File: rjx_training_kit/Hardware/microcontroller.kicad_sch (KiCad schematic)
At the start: 15 parts, among them SW2 SW_Push, U9 STM32L431RCTx, Y1 8MHz

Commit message: [RJX]: Initial footprint assignment. This is subject to further review and analysis.
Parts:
- C15, C16, C17, C18, C19, C20, C21, C22, C23, C24, C25: footprint (none) -> Capacitor_SMD:C_0603_1608Metric
- R41: footprint (none) -> Resistor_SMD:R_0603_1608Metric
- SW2: footprint (none) -> Button_Switch_THT:SW_PUSH_6mm
- Y1: footprint (none) -> Crystal:Crystal_SMD_3225-4Pin_3.2x2.5mm
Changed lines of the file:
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@@
 			)
 		)
-		(property "Footprint" ""
+		(property "Footprint" "Capacitor_SMD:C_0603_1608Metric"
 			(at 86.6648 52.07 0)
 			(effects
@@
 			)
 		)
-		(property "Footprint" ""
+		(property "Footprint" "Capacitor_SMD:C_0603_1608Metric"
 			(at 47.2948 80.01 0)
 			(effects
@@
 			)
 		)
-		(property "Footprint" ""
+		(property "Footprint" "Capacitor_SMD:C_0603_1608Metric"
 			(at 68.8848 96.52 0)
 			(effects
@@
 			)
 		)
-		(property "Footprint" ""
+		(property "Footprint" "Crystal:Crystal_SMD_3225-4Pin_3.2x2.5mm"
 			(at 62.23 85.09 0)
 			(effects
@@
 			)
 		)
-		(property "Footprint" ""
+		(property "Footprint" "Capacitor_SMD:C_0603_1608Metric"
 			(at 53.6448 96.52 0)
 			(effects
@@
 			)
 		)
-		(property "Footprint" ""
+		(property "Footprint" "Resistor_SMD:R_0603_1608Metric"
 			(at 86.614 85.344 90)
 			(effects
@@
 			)
 		)
-		(property "Footprint" ""
+		(property "Footprint" "Capacitor_SMD:C_0603_1608Metric"
 			(at 132.3848 52.07 0)
 			(effects
@@
 			)
 		)
-		(property "Footprint" ""
+		(property "Footprint" "Capacitor_SMD:C_0603_1608Metric"
 			(at 120.9548 52.07 0)
 			(effects
@@
 			)
 		)
-		(property "Footprint" ""
+		(property "Footprint" "Capacitor_SMD:C_0603_1608Metric"
 			(at 98.0948 52.07 0)
 			(effects
@@
 			)
 		)
-		(property "Footprint" ""
+		(property "Footprint" "Capacitor_SMD:C_0603_1608Metric"
 			(at 174.2948 52.07 0)
 			(effects
@@
 			)
 		)
-		(property "Footprint" ""
+		(property "Footprint" "Capacitor_SMD:C_0603_1608Metric"
 			(at 109.5248 52.07 0)
 			(effects
@@
 			)
 		)
-		(property "Footprint" ""
+		(property "Footprint" "Button_Switch_THT:SW_PUSH_6mm"
 			(at 33.02 76.2 0)
 			(effects
@@
 			)
 		)
-		(property "Footprint" ""
+		(property "Footprint" "Capacitor_SMD:C_0603_1608Metric"
 			(at 164.1348 52.07 0)
 			(effects
@@
 			)
 		)
-		(property "Footprint" ""
+		(property "Footprint" "Capacitor_SMD:C_0603_1608Metric"
 			(at 143.8148 52.07 0)
 			(effects

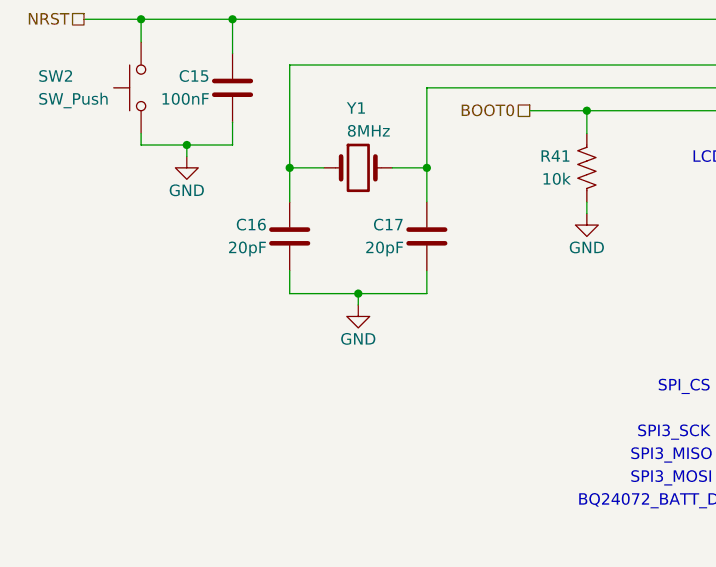
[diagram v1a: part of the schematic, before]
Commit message: [RJX]: Updated load capacitance values
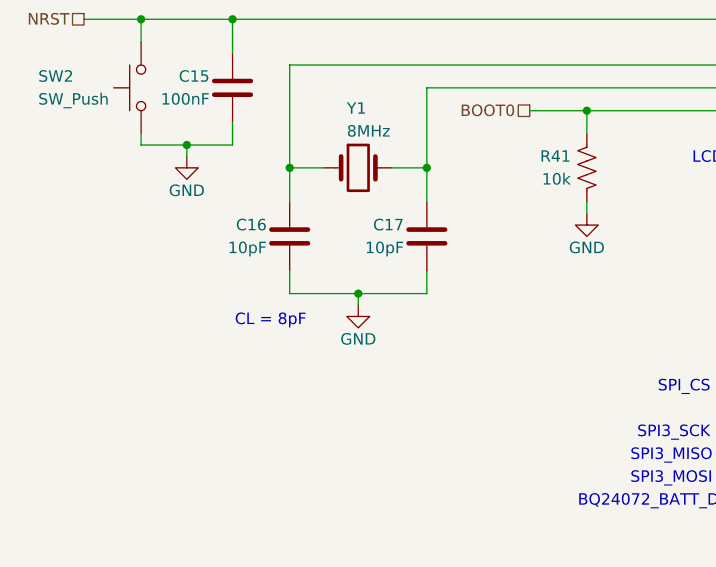
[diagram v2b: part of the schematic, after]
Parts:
- C16, C17: value 20pF -> 10pF
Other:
- note added: "CL = 8pF"
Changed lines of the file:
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@@
+		)
+	)
+	(text "CL = 8pF"
+		(exclude_from_sim no)
+		(at 48.514 102.108 0)
+		(effects
+			(font
+				(size 1.27 1.27)
+			)
+			(justify left)
 		)
 	)
@@
 			)
 		)
-		(property "Value" "20pF"
+		(property "Value" "10pF"
 			(at 67.31 93.98 0)
 			(effects
@@
 			)
 		)
-		(property "Value" "20pF"
+		(property "Value" "10pF"
 			(at 52.07 93.98 0)
 			(effects

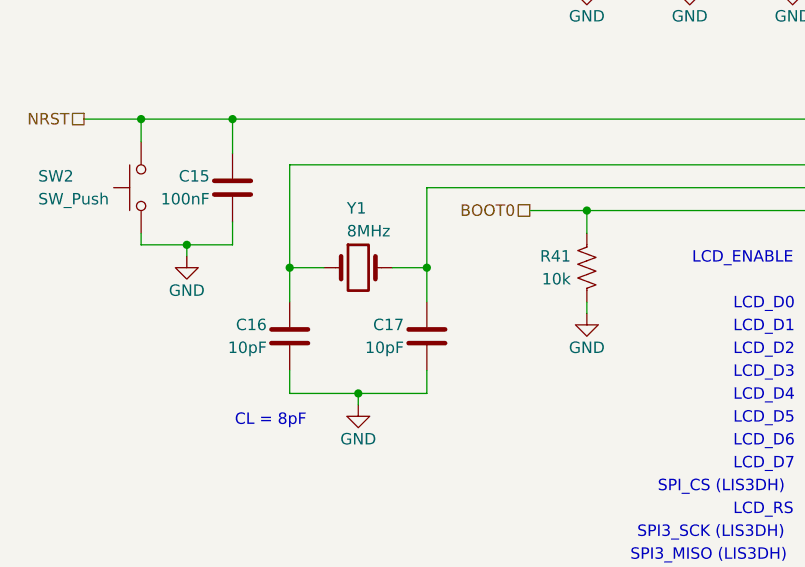
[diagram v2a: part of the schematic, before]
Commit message: [RJX]: Schematic, Netlist, and PCB update. Replaced 2-pin crystal with 4-pin passive crystal.
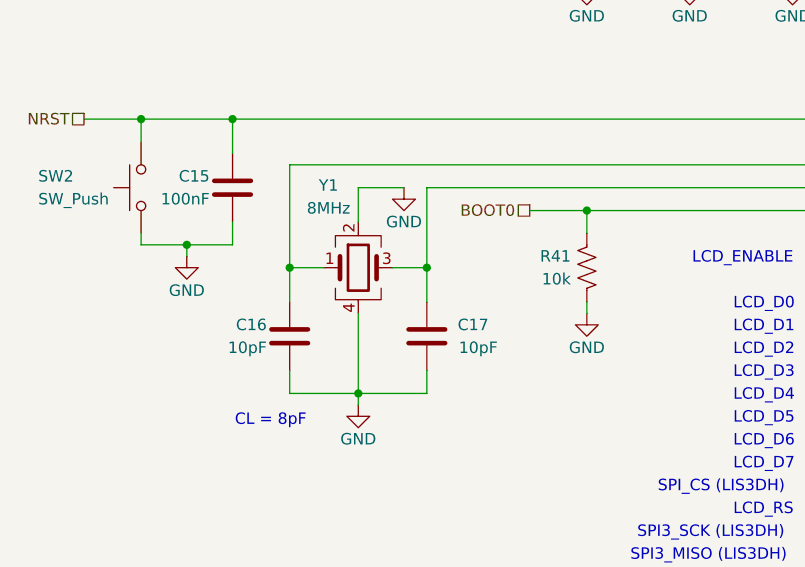
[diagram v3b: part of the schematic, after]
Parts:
- removed Y1: 8MHz, Crystal:Crystal_SMD_3225-4Pin_3.2x2.5mm, symbol Device:Crystal
- added Y1: 8MHz, Crystal:Crystal_SMD_3225-4Pin_3.2x2.5mm, symbol Device:Crystal_GND24
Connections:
- net GND: now also Y1.2, Y1.4
- net at C17.1, U9.6 (PH1): now also Y1.3
- net at C16.1, U9.5 (PH0): now also Y1.1
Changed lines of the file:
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@@
+	(wire
+		(pts
+			(xy 62.23 80.01) (xy 62.23 76.2)
+		)
+		(stroke
+			(width 0)
+			(type default)
+		)
+	)
 	(wire
 		(pts
@@
 	(wire
 		(pts
+			(xy 62.23 76.2) (xy 67.31 76.2)
+		)
+		(stroke
+			(width 0)
+			(type default)
+		)
+	)
+	(wire
+		(pts
 			(xy 165.1 124.46) (xy 175.26 124.46)
 		)
@@
 		(pts
 			(xy 165.1 132.08) (xy 175.26 132.08)
+		)
+		(stroke
+			(width 0)
+			(type default)
+		)
+	)
+	(wire
+		(pts
+			(xy 62.23 90.17) (xy 62.23 99.06)
 		)
 		(stroke
@@
 		(dnp no)
 		(property "Reference" "C17"
-			(at 67.31 91.44 0)
+			(at 76.708 91.44 0)
 			(effects
 				(font
@@
 		)
 		(property "Value" "10pF"
-			(at 67.31 93.98 0)
+			(at 77.724 93.98 0)
 			(effects
 				(font
@@
 	)
 	(symbol
-		(lib_id "Device:Crystal")
+		(lib_id "Device:Crystal_GND24")
 		(at 62.23 85.09 0)
 		(unit 1)
@@
 		(dnp no)
 		(property "Reference" "Y1"
-			(at 60.96 78.486 0)
-			(effects
-				(font
-					(size 1.27 1.27)
-				)
-				(justify left)
+			(at 58.928 75.946 0)
+			(effects
+				(font
+					(size 1.27 1.27)
+				)
 			)
 		)
 		(property "Value" "8MHz"
-			(at 60.96 81.026 0)
-			(effects
-				(font
-					(size 1.27 1.27)
-				)
-				(justify left)
+			(at 58.928 78.486 0)
+			(effects
+				(font
+					(size 1.27 1.27)
+				)
 			)
 		)
@@
 			)
 		)
-		(property "Description" "Two pin crystal"
+		(property "Description" "Four pin crystal, GND on pins 2 and 4"
 			(at 62.23 85.09 0)
 			(effects
@@
 			)
 		)
+		(pin "4"
+		)
+		(pin "3"
+		)
+		(pin "1"
+		)
 		(pin "2"
 		)
-		(pin "1"
-		)
 		(instances
-			(project "rjx_training_kit"
+			(project ""
 				(path "/c10d0f5f-1570-4ced-80f8-bf69ea514c66/6ff37231-b90f-440e-bce5-b002d3bf6e3d"
 					(reference "Y1")
@@
 					(unit 1)
 				)
+			)
+		)
+	)
+	(symbol
+		(lib_id "power:GND")
+		(at 67.31 76.2 0)
+		(unit 1)
+		(exclude_from_sim no)
+		(in_bom yes)
+		(on_board yes)
+		(dnp no)
+		(property "Reference" "#PWR087"
+			(at 67.31 82.55 0)
+			(effects
+				(font
+					(size 1.27 1.27)
+				)
+				(hide yes)
+			)
+		)
+		(property "Value" "GND"
+			(at 67.31 80.01 0)
+			(effects
+				(font
+					(size 1.27 1.27)
+				)
+			)
+		)
+		(property "Footprint" ""
+			(at 67.31 76.2 0)
+			(effects
+				(font
+					(size 1.27 1.27)
+				)
+				(hide yes)
+			)
+		)
+		(property "Datasheet" ""
+			(at 67.31 76.2 0)
+			(effects
+				(font
+					(size 1.27 1.27)
+				)
+				(hide yes)
+			)
+		)
+		(property "Description" "Power symbol creates a global label with name \"GND\" , ground"
+			(at 67.31 76.2 0)
+			(effects
+				(font
+					(size 1.27 1.27)
+				)
+				(hide yes)
+			)
+		)
+		(pin "1"
+		)
+		(instances
+			(project "rjx_training_kit"
+				(path "/c10d0f5f-1570-4ced-80f8-bf69ea514c66/6ff37231-b90f-440e-bce5-b002d3bf6e3d"
+					(reference "#PWR087")
+					(unit 1)
+				)
